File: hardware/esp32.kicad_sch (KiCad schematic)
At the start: 27 parts, among them U2 USBLC6-2SC6

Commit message: updated files
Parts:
- removed ESP_B0: SW_SPDT, Button_Switch_SMD:SW_SPDT_PCM12, symbol Switch:SW_SPDT
- removed R17, R18: 10, Resistor_SMD:R_0402_1005Metric, symbol Device:R
- added ESP_B0: SS-3292S-L2-B, SS-3292S-L2-B:SW-SMD_SS-3292S-L2-B, symbol SS-3292S-L2-B:SS-3292S-L2-B
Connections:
- net ESP32-GPIO0: now also ESP_B0.2
- net ESP32-RGB_IN: now also ESP32-S3.25 (IO21); no longer ESP32-S3.44 (IO46)
- net GND: now also ESP_B0.1, ESP_B0.EH
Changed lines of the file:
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@@
 	)
 	(no_connect
-		(at 55.88 143.51)
+		(at 55.88 135.89)
 	)
 	(wire
@@
 	(wire
 		(pts
-			(xy 43.18 140.97) (xy 45.72 140.97)
-		)
-		(stroke
-			(width 0)
-			(type default)
-		)
-	)
-	(wire
-		(pts
 			(xy 100.33 135.89) (xy 100.33 134.62)
 		)
@@
 	(wire
 		(pts
-			(xy 160.02 176.53) (xy 154.94 176.53)
-		)
-		(stroke
-			(width 0.5)
-			(type solid)
-			(color 255 0 0 1)
-		)
-	)
-	(wire
-		(pts
-			(xy 147.32 176.53) (xy 142.24 176.53)
+			(xy 142.24 176.53) (xy 160.02 176.53)
 		)
 		(stroke
@@
 	(wire
 		(pts
-			(xy 43.18 140.97) (xy 43.18 147.32)
-		)
-		(stroke
-			(width 0)
-			(type default)
-		)
-	)
-	(wire
-		(pts
 			(xy 25.4 121.92) (xy 25.4 124.46)
 		)
@@
 	(wire
 		(pts
-			(xy 160.02 173.99) (xy 154.94 173.99)
-		)
-		(stroke
-			(width 0.5)
-			(type solid)
-			(color 255 0 0 1)
-		)
-	)
-	(wire
-		(pts
 			(xy 95.25 148.59) (xy 95.25 144.78)
 		)
@@
 	(wire
 		(pts
-			(xy 147.32 173.99) (xy 142.24 173.99)
+			(xy 142.24 173.99) (xy 160.02 173.99)
 		)
 		(stroke
@@
 		)
 	)
+	(global_label "ESP32-RGB_IN"
+		(shape input)
+		(at 123.19 50.8 0)
+		(fields_autoplaced yes)
+		(effects
+			(font
+				(size 1.27 1.27)
+			)
+			(justify left)
+		)
+		(property "Intersheetrefs" "${INTERSHEET_REFS}"
+			(at 140.508 50.8 0)
+			(effects
+				(font
+					(size 1.27 1.27)
+				)
+				(justify left)
+				(hide yes)
+			)
+		)
+	)
 	(global_label "RFD_900"
 		(shape input)
@@
 		)
 	)
-	(global_label "ESP32-RGB_IN"
-		(shape input)
-		(at 123.19 83.82 0)
-		(fields_autoplaced yes)
-		(effects
-			(font
-				(size 1.27 1.27)
-			)
-			(justify left)
-		)
-		(property "Intersheetrefs" "${INTERSHEET_REFS}"
-			(at 140.508 83.82 0)
-			(effects
-				(font
-					(size 1.27 1.27)
-				)
-				(justify left)
-				(hide yes)
-			)
-		)
-	)
 	(global_label "ESP32-RX1"
 		(shape input)
@@
 	(symbol
 		(lib_id "power:GND")
-		(at 43.18 147.32 0)
+		(at 55.88 140.97 0)
 		(unit 1)
 		(exclude_from_sim no)
@@
 		(fields_autoplaced yes)
 		(property "Reference" "#PWR017"
-			(at 43.18 153.67 0)
+			(at 55.88 147.32 0)
 			(effects
 				(font
@@
 		)
 		(property "Value" "GND"
-			(at 43.18 151.13 90)
+			(at 55.88 144.78 90)
 			(effects
 				(font
@@
 		)
 		(property "Footprint" ""
-			(at 43.18 147.32 0)
+			(at 55.88 140.97 0)
 			(effects
 				(font
@@
 		)
 		(property "Datasheet" ""
-			(at 43.18 147.32 0)
+			(at 55.88 140.97 0)
 			(effects
 				(font
@@
 		)
 		(property "Description" ""
-			(at 43.18 147.32 0)
+			(at 55.88 140.97 0)
 			(effects
 				(font
@@
 	)
 	(symbol
-		(lib_id "Device:R")
-		(at 151.13 176.53 90)
-		(unit 1)
-		(exclude_from_sim no)
-		(in_bom yes)
-		(on_board yes)
-		(dnp no)
-		(property "Reference" "R18"
-			(at 151.13 179.07 90)
-			(effects
-				(font
-					(size 1.27 1.27)
-				)
-			)
-		)
-		(property "Value" "10"
-			(at 151.13 176.53 90)
-			(effects
-				(font
-					(size 1.27 1.27)
-				)
-			)
-		)
-		(property "Footprint" "Resistor_SMD:R_0402_1005Metric"
-			(at 151.13 178.308 90)
-			(effects
-				(font
-					(size 1.27 1.27)
-				)
-				(hide yes)
-			)
-		)
-		(property "Datasheet" "~"
-			(at 151.13 176.53 0)
-			(effects
-				(font
-					(size 1.27 1.27)
-				)
-				(hide yes)
-			)
-		)
-		(property "Description" ""
-			(at 151.13 176.53 0)
-			(effects
-				(font
-					(size 1.27 1.27)
-				)
-				(hide yes)
-			)
-		)
-		(pin "1"
-		)
-		(pin "2"
-		)
-		(instances
-			(project "aether"
-				(path "/e12346fa-509d-4de9-8ab1-dced307292db/a5bc5271-f6b1-46bc-807d-d0d88ce9901f"
-					(reference "R18")
-					(unit 1)
-				)
-			)
-		)
-	)
-	(symbol
 		(lib_id "Device:C")
 		(at 63.5 35.56 0)
@@
 	)
 	(symbol
-		(lib_id "Switch:SW_SPDT")
-		(at 50.8 140.97 0)
+		(lib_id "power:GND")
+		(at 45.72 138.43 0)
 		(unit 1)
 		(exclude_from_sim no)
@@
 		(dnp no)
 		(fields_autoplaced yes)
-		(property "Reference" "ESP_B0"
-			(at 50.8 132.08 0)
+		(property "Reference" "#PWR019"
+			(at 45.72 144.78 0)
 			(effects
 				(font
 					(size 1.27 1.27)
 				)
+				(hide yes)
 			)
 		)
-		(property "Value" "SW_SPDT"
-			(at 50.8 134.62 0)
+		(property "Value" "GND"
+			(at 45.72 142.24 90)
 			(effects
 				(font
 					(size 1.27 1.27)
 				)
+				(justify right)
+				(hide yes)
 			)
 		)
-		(property "Footprint" "Button_Switch_SMD:SW_SPDT_PCM12"
-			(at 50.8 140.97 0)
+		(property "Footprint" ""
+			(at 45.72 138.43 0)
 			(effects
 				(font
@@
 			)
 		)
-		(property "Datasheet" "~"
-			(at 50.8 148.59 0)
+		(property "Datasheet" ""
+			(at 45.72 138.43 0)
 			(effects
 				(font
@@
 			)
 		)
-		(property "Description" "Switch, single pole double throw"
-			(at 50.8 140.97 0)
+		(property "Description" ""
+			(at 45.72 138.43 0)
 			(effects
 				(font
@@
 			)
 		)
-		(pin "3"
-		)
-		(pin "2"
-		)
 		(pin "1"
 		)
@@
 			(project "aether"
 				(path "/e12346fa-509d-4de9-8ab1-dced307292db/a5bc5271-f6b1-46bc-807d-d0d88ce9901f"
-					(reference "ESP_B0")
+					(reference "#PWR019")
 					(unit 1)
 				)
@@
 	(symbol
 		(lib_id "Device:R")
-		(at 151.13 173.99 90)
-		(unit 1)
-		(exclude_from_sim no)
-		(in_bom yes)
-		(on_board yes)
-		(dnp no)
-		(property "Reference" "R17"
-			(at 151.13 171.45 90)
-			(effects
-				(font
-					(size 1.27 1.27)
-				)
-			)
-		)
-		(property "Value" "10"
-			(at 151.13 173.99 90)
-			(effects
-				(font
-					(size 1.27 1.27)
-				)
-			)
-		)
-		(property "Footprint" "Resistor_SMD:R_0402_1005Metric"
-			(at 151.13 175.768 90)
-			(effects
-				(font
-					(size 1.27 1.27)
-				)
-				(hide yes)
-			)
-		)
-		(property "Datasheet" "~"
-			(at 151.13 173.99 0)
-			(effects
-				(font
-					(size 1.27 1.27)
-				)
-				(hide yes)
-			)
-		)
-		(property "Description" ""
-			(at 151.13 173.99 0)
-			(effects
-				(font
-					(size 1.27 1.27)
-				)
-				(hide yes)
-			)
-		)
-		(pin "1"
-		)
-		(pin "2"
-		)
-		(instances
-			(project "aether"
-				(path "/e12346fa-509d-4de9-8ab1-dced307292db/a5bc5271-f6b1-46bc-807d-d0d88ce9901f"
-					(reference "R17")
-					(unit 1)
-				)
-			)
-		)
-	)
-	(symbol
-		(lib_id "Device:R")
 		(at 100.33 128.27 180)
 		(unit 1)
@@
 					(unit 1)
 				)
+			)
+		)
+	)
+	(symbol
+		(lib_id "SS-3292S-L2-B:SS-3292S-L2-B")
+		(at 52.07 138.43 90)
+		(unit 1)
+		(exclude_from_sim no)
+		(in_bom yes)
+		(on_board yes)
+		(dnp no)
+		(property "Reference" "ESP_B0"
+			(at 50.8 131.318 90)
+			(effects
+				(font
+					(size 1.27 1.27)
+				)
+			)
+		)
+		(property "Value" "SS-3292S-L2-B"
+			(at 50.8 130.81 90)
+			(effects
+				(font
+					(size 1.27 1.27)
+				)
+				(hide yes)
+			)
+		)
+		(property "Footprint" "SS-3292S-L2-B:SW-SMD_SS-3292S-L2-B"
+			(at 62.23 138.43 0)
+			(effects
+				(font
+					(size 1.27 1.27)
+					(italic yes)
+				)
+				(hide yes)
+			)
+		)
+		(property "Datasheet" "https://item.szlcsc.com/512183.html?ref=editor&logined=true"
+			(at 51.943 140.716 0)
+			(effects
+				(font
+					(size 1.27 1.27)
+				)
+				(justify left)
+				(hide yes)
+			)
+		)
+		(property "Description" ""
+			(at 52.07 138.43 0)
+			(effects
+				(font
+					(size 1.27 1.27)
+				)
+				(hide yes)
+			)
+		)
+		(property "LCSC" "C500057"
+			(at 52.07 138.43 0)
+			(effects
+				(font
+					(size 1.27 1.27)
+				)
+				(hide yes)
+			)
+		)
+		(pin "2"
+		)
+		(pin "1"
+		)
+		(pin "3"
+		)
+		(pin "EH"
+		)
+		(instances
+			(project ""
+				(path "/e12346fa-509d-4de9-8ab1-dced307292db/a5bc5271-f6b1-46bc-807d-d0d88ce9901f"
+					(reference "ESP_B0")
+					(unit 1)
+				)

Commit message: updated routing
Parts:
- D4: value LED -> YELLOW
- D5: value LED -> BLUE
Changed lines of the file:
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@@
 			)
 		)
-		(property "Value" "LED"
+		(property "Value" "BLUE"
 			(at 241.6175 60.96 90)
 			(effects
@@
 			)
 		)
-		(property "Value" "LED"
+		(property "Value" "YELLOW"
 			(at 241.6175 69.85 90)
 			(effects

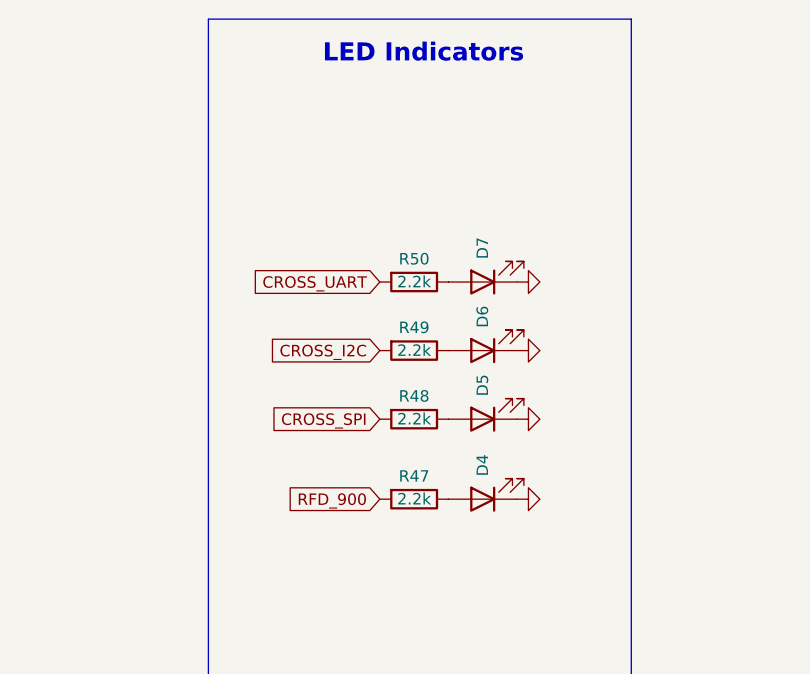
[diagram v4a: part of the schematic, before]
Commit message: Updated minimum via hole size to 0.3mm.
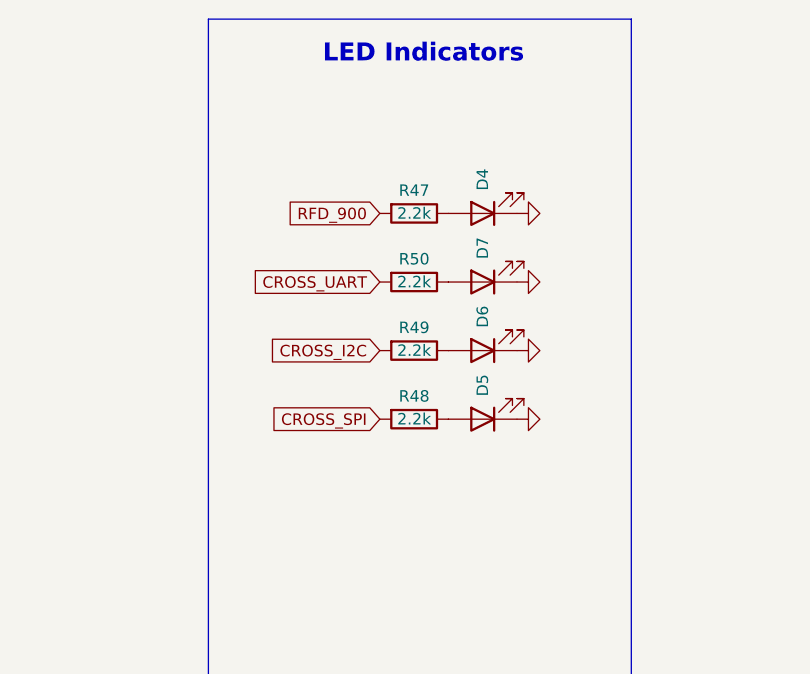
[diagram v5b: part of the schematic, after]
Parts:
- D4: value YELLOW -> RUBY RED
- D5: value BLUE -> ROYAL BLUE
- D6: value LED -> EMERALD GREEN
- D7: value LED -> ORANGE
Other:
- moved on the sheet: D4, R47
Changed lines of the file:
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@@
 	(global_label "RFD_900"
 		(shape input)
-		(at 227.33 73.66 180)
+		(at 227.33 41.91 180)
 		(fields_autoplaced yes)
 		(effects
@@
 		)
 		(property "Intersheetrefs" "${INTERSHEET_REFS}"
-			(at 216.1201 73.66 0)
+			(at 216.1201 41.91 0)
 			(effects
 				(font
@@
 			)
 		)
-		(property "Value" "BLUE"
+		(property "Value" "ROYAL BLUE"
 			(at 241.6175 60.96 90)
 			(effects
@@
 			)
 		)
-		(property "Value" "LED"
+		(property "Value" "EMERALD GREEN"
 			(at 241.6175 53.34 90)
 			(effects
@@
 	(symbol
 		(lib_id "Device:R")
-		(at 231.14 73.66 270)
+		(at 231.14 41.91 270)
 		(unit 1)
 		(exclude_from_sim no)
@@
 		(dnp no)
 		(property "Reference" "R47"
-			(at 231.14 71.12 90)
+			(at 231.14 39.37 90)
 			(effects
 				(font
@@
 		)
 		(property "Value" "2.2k"
-			(at 231.14 73.66 90)
+			(at 231.14 41.91 90)
 			(effects
 				(font
@@
 		)
 		(property "Footprint" "Resistor_SMD:R_0603_1608Metric"
-			(at 231.14 71.882 90)
+			(at 231.14 40.132 90)
 			(effects
 				(font
@@
 		)
 		(property "Datasheet" "~"
-			(at 231.14 73.66 0)
+			(at 231.14 41.91 0)
 			(effects
 				(font
@@
 		)
 		(property "Description" ""
-			(at 231.14 73.66 0)
+			(at 231.14 41.91 0)
 			(effects
 				(font
@@
 	(symbol
 		(lib_id "Device:LED")
-		(at 238.76 73.66 180)
+		(at 238.76 41.91 180)
 		(unit 1)
 		(exclude_from_sim no)
@@
 		(dnp no)
 		(property "Reference" "D4"
-			(at 238.76 71.12 90)
+			(at 238.76 39.37 90)
 			(effects
 				(font
@@
 			)
 		)
-		(property "Value" "YELLOW"
-			(at 241.6175 69.85 90)
+		(property "Value" "RUBY RED"
+			(at 241.6175 38.1 90)
 			(effects
 				(font
@@
 		)
 		(property "Footprint" "LED_SMD:LED_0603_1608Metric"
-			(at 238.76 73.66 0)
+			(at 238.76 41.91 0)
 			(effects
 				(font
@@
 		)
 		(property "Datasheet" "~"
-			(at 238.76 73.66 0)
+			(at 238.76 41.91 0)
 			(effects
 				(font
@@
 		)
 		(property "Description" ""
-			(at 238.76 73.66 0)
+			(at 238.76 41.91 0)
 			(effects
 				(font
@@
 	(symbol
 		(lib_id "power:GND")
-		(at 242.57 73.66 90)
+		(at 242.57 41.91 90)
 		(unit 1)
 		(exclude_from_sim no)
@@
 		(fields_autoplaced yes)
 		(property "Reference" "#PWR01"
-			(at 248.92 73.66 0)
+			(at 248.92 41.91 0)
 			(effects
 				(font
@@
 		)
 		(property "Value" "GND"
-			(at 246.38 73.66 90)
+			(at 246.38 41.91 90)
 			(effects
 				(font
@@
 		)
 		(property "Footprint" ""
-			(at 242.57 73.66 0)
+			(at 242.57 41.91 0)
 			(effects
 				(font
@@
 		)
 		(property "Datasheet" ""
-			(at 242.57 73.66 0)
+			(at 242.57 41.91 0)
 			(effects
 				(font
@@
 		)
 		(property "Description" ""
-			(at 242.57 73.66 0)
+			(at 242.57 41.91 0)
 			(effects
 				(font
@@
 			)
 		)
-		(property "Value" "LED"
+		(property "Value" "ORANGE"
 			(at 241.6175 45.72 90)
 			(effects
